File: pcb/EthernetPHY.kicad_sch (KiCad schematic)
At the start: 24 parts, among them U1 W5500, Y2 3225-25M-SR

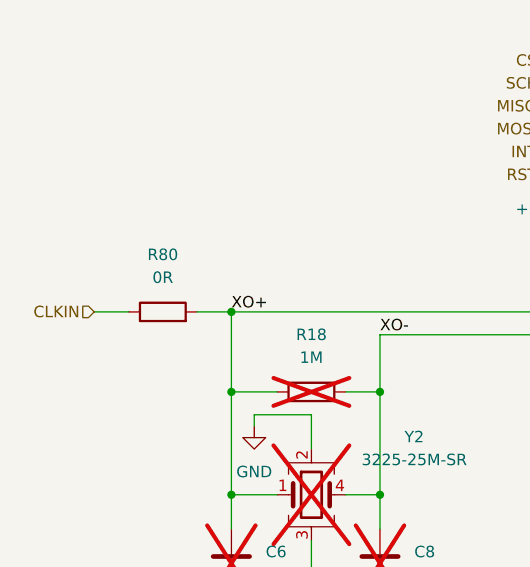
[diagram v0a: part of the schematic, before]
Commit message: Added SI5351C
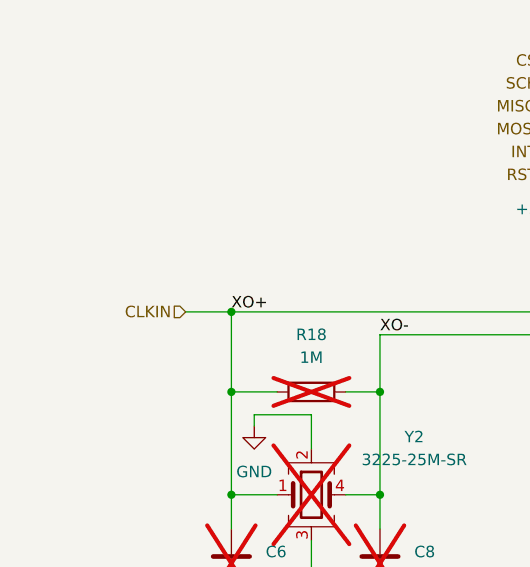
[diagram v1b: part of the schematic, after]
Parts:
- removed R80: 0R, Resistor_SMD:R_0402_1005Metric_Pad0.72x0.64mm_HandSolder, symbol Device:R
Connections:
- net XO+ is gone; now on net CLKIN: C6.1, R18.1, U1.30 (XI/CLKIN), Y2.1
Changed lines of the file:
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@@
-	(wire
-		(pts
-			(xy 73.66 93.98) (xy 77.47 93.98)
-		)
-		(stroke
-			(width 0)
-			(type default)
-		)
-	)
 	(wire
 		(pts
@@
 	(wire
 		(pts
-			(xy 62.23 93.98) (xy 66.04 93.98)
+			(xy 72.39 93.98) (xy 77.47 93.98)
 		)
 		(stroke
@@
 	(hierarchical_label "CLKIN"
 		(shape input)
-		(at 62.23 93.98 180)
+		(at 72.39 93.98 180)
 		(effects
 			(font
@@
 					(unit 1)
 				)
-			)
-		)
-	)
-	(symbol
-		(lib_id "Device:R")
-		(at 69.85 93.98 90)
-		(unit 1)
-		(exclude_from_sim no)
-		(in_bom yes)
-		(on_board yes)
-		(dnp no)
-		(fields_autoplaced yes)
-		(property "Reference" "R80"
-			(at 69.85 87.63 90)
-			(effects
-				(font
-					(size 1.27 1.27)
-				)
-			)
-		)
-		(property "Value" "0R"
-			(at 69.85 90.17 90)
-			(effects
-				(font
-					(size 1.27 1.27)
-				)
-			)
-		)
-		(property "Footprint" "Resistor_SMD:R_0402_1005Metric_Pad0.72x0.64mm_HandSolder"
-			(at 69.85 95.758 90)
-			(effects
-				(font
-					(size 1.27 1.27)
-				)
-				(hide yes)
-			)
-		)
-		(property "Datasheet" "~"
-			(at 69.85 93.98 0)
-			(effects
-				(font
-					(size 1.27 1.27)
-				)
-				(hide yes)
-			)
-		)
-		(property "Description" "Resistor"
-			(at 69.85 93.98 0)
-			(effects
-				(font
-					(size 1.27 1.27)
-				)
-				(hide yes)
-			)
-		)
-		(pin "1"
-		)
-		(pin "2"
-		)
-		(instances
-			(project ""
-				(path "/0c4edb77-9bdf-4103-be66-c5eb9940b163/7e1fd6ab-9257-4fb8-b441-cd2451b29cbb"
-					(reference "R80")
-					(unit 1)
-				)

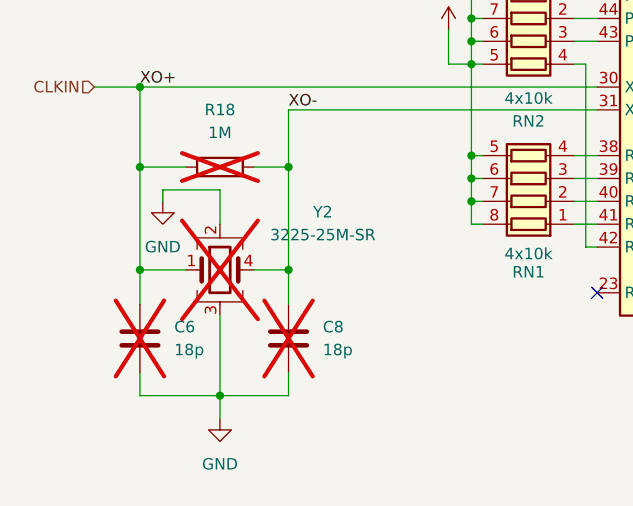
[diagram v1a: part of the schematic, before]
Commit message: Crystal footprint changed, routing and eth trafo to correct
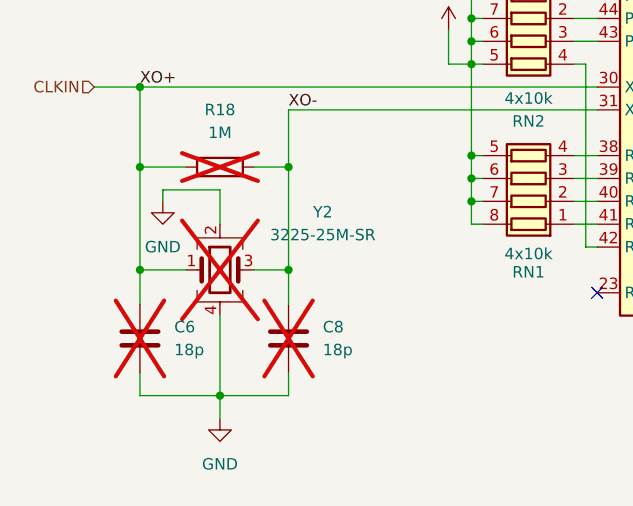
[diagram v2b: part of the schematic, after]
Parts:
- Y2: symbol Device:Crystal_GND23 -> Device:Crystal_GND24
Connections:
- net GND: now also Y2.4; no longer Y2.3
- net XO-: now also Y2.3; no longer Y2.4
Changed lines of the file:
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@@
 	)
 	(symbol
-		(lib_id "Device:Crystal_GND23")
+		(lib_id "Device:Crystal_GND24")
 		(at 86.36 114.3 0)
 		(unit 1)
@@
 			)
 		)
-		(property "Description" "Four pin crystal, GND on pins 2 and 3"
+		(property "Description" "Four pin crystal, GND on pins 2 and 4"
 			(at 86.36 114.3 0)
 			(effects

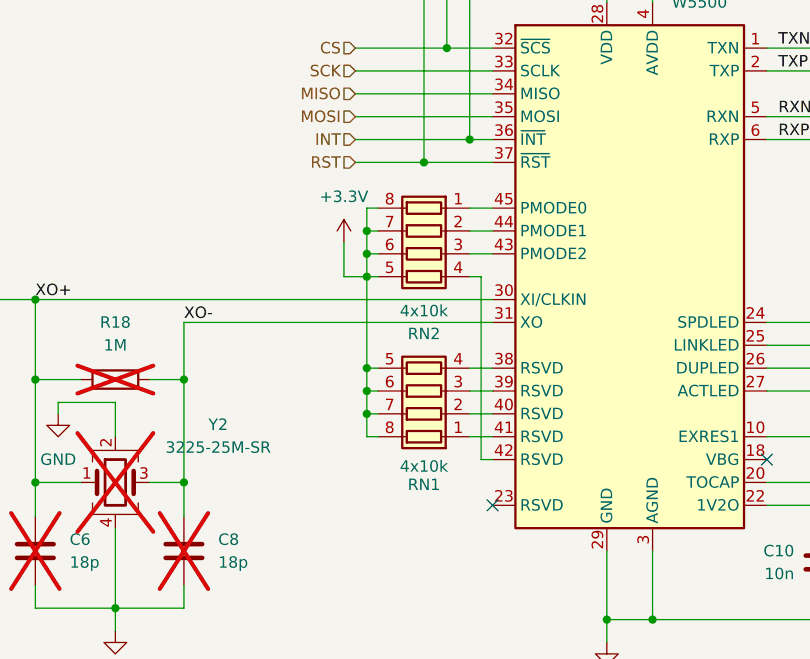
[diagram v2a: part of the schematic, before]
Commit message: Corected mistakes found on RDE_board
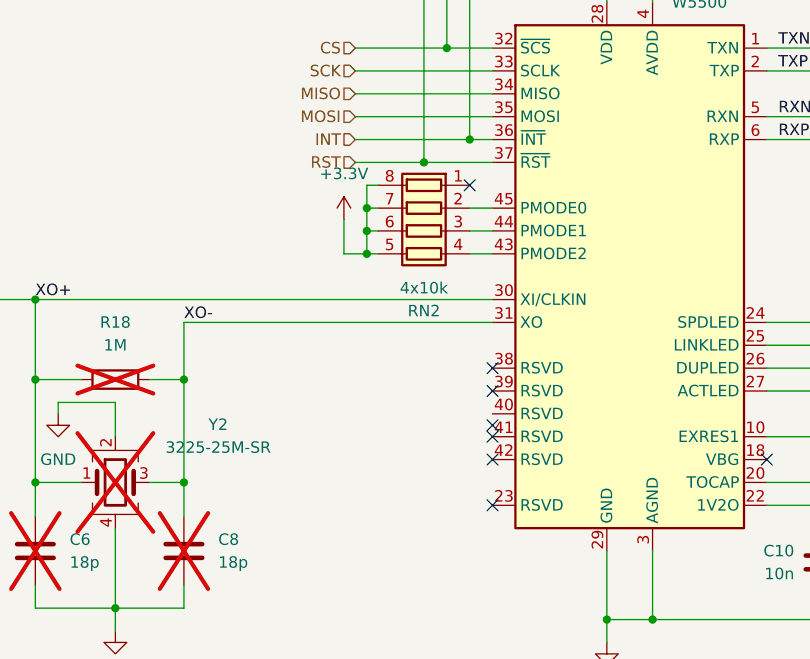
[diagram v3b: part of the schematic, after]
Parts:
- removed RN1: 4x10k, Resistor_SMD:R_Array_Convex_4x0603, symbol Device:R_Pack04
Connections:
- net at RN2.1 (R1.1): no longer U1.45 (PMODE0)
- net at RN2.2 (R2.1): now also U1.45 (PMODE0); no longer U1.44 (PMODE1)
- net at RN2.3 (R3.1): now also U1.44 (PMODE1); no longer U1.43 (PMODE2)
- net at RN2.4 (R4.1): now also U1.43 (PMODE2); no longer U1.42 (RSVD)
- no-connect marks 3 -> 9
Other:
- moved on the sheet: RN2
